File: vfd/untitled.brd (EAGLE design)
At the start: 128.9 x 185.7 mm, 80 parts, among them IC1 FSBB30CH60, IC2 74HCT04D, T1 BC547, X3 5202-06-N-02

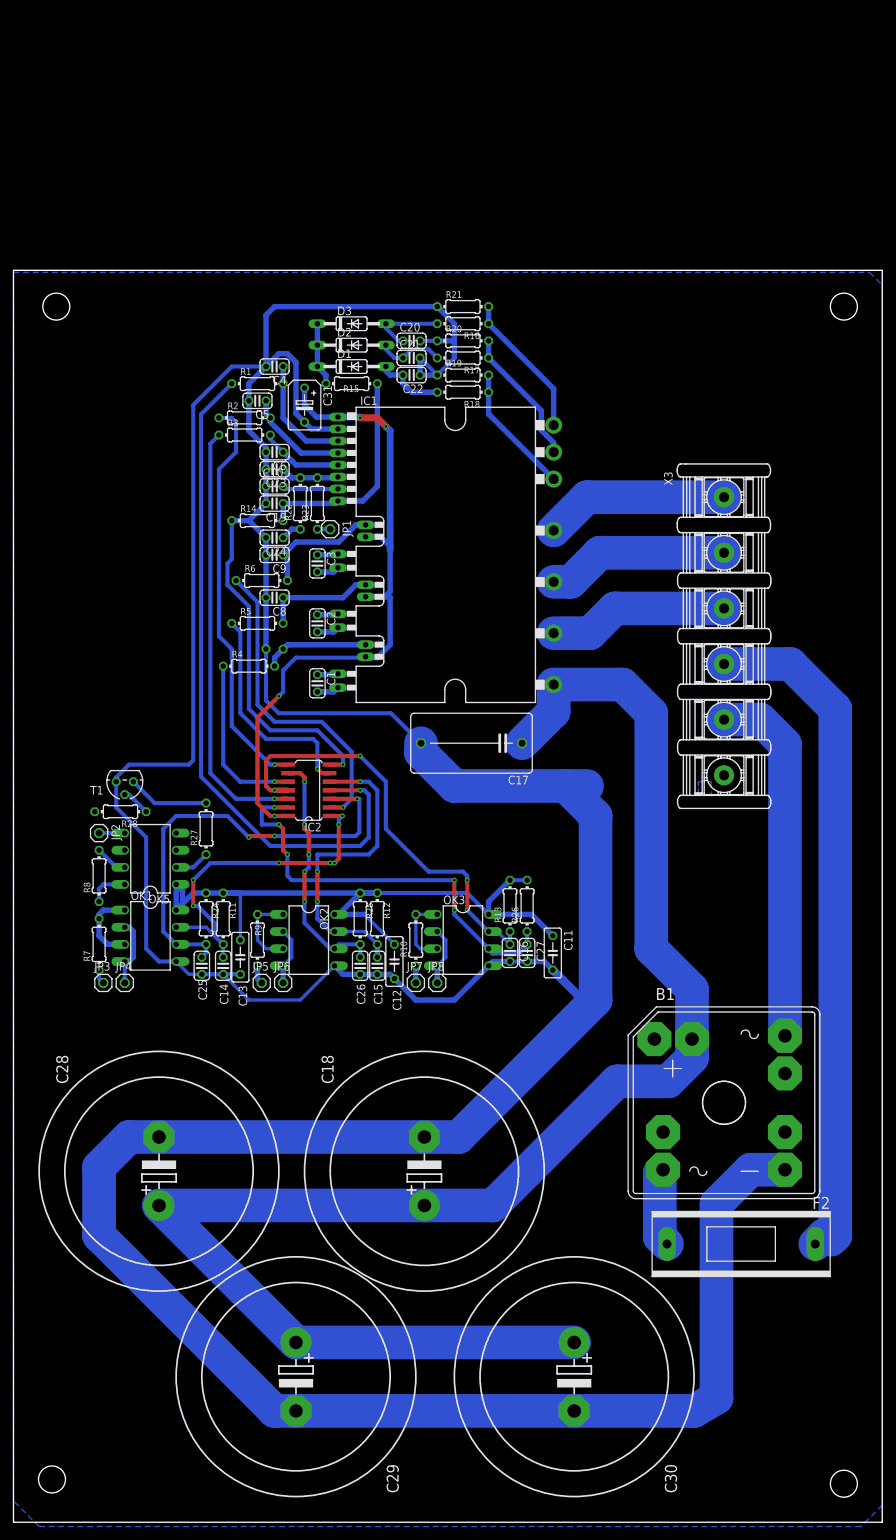
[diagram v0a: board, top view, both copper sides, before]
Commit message: update trafo
trafo 15v
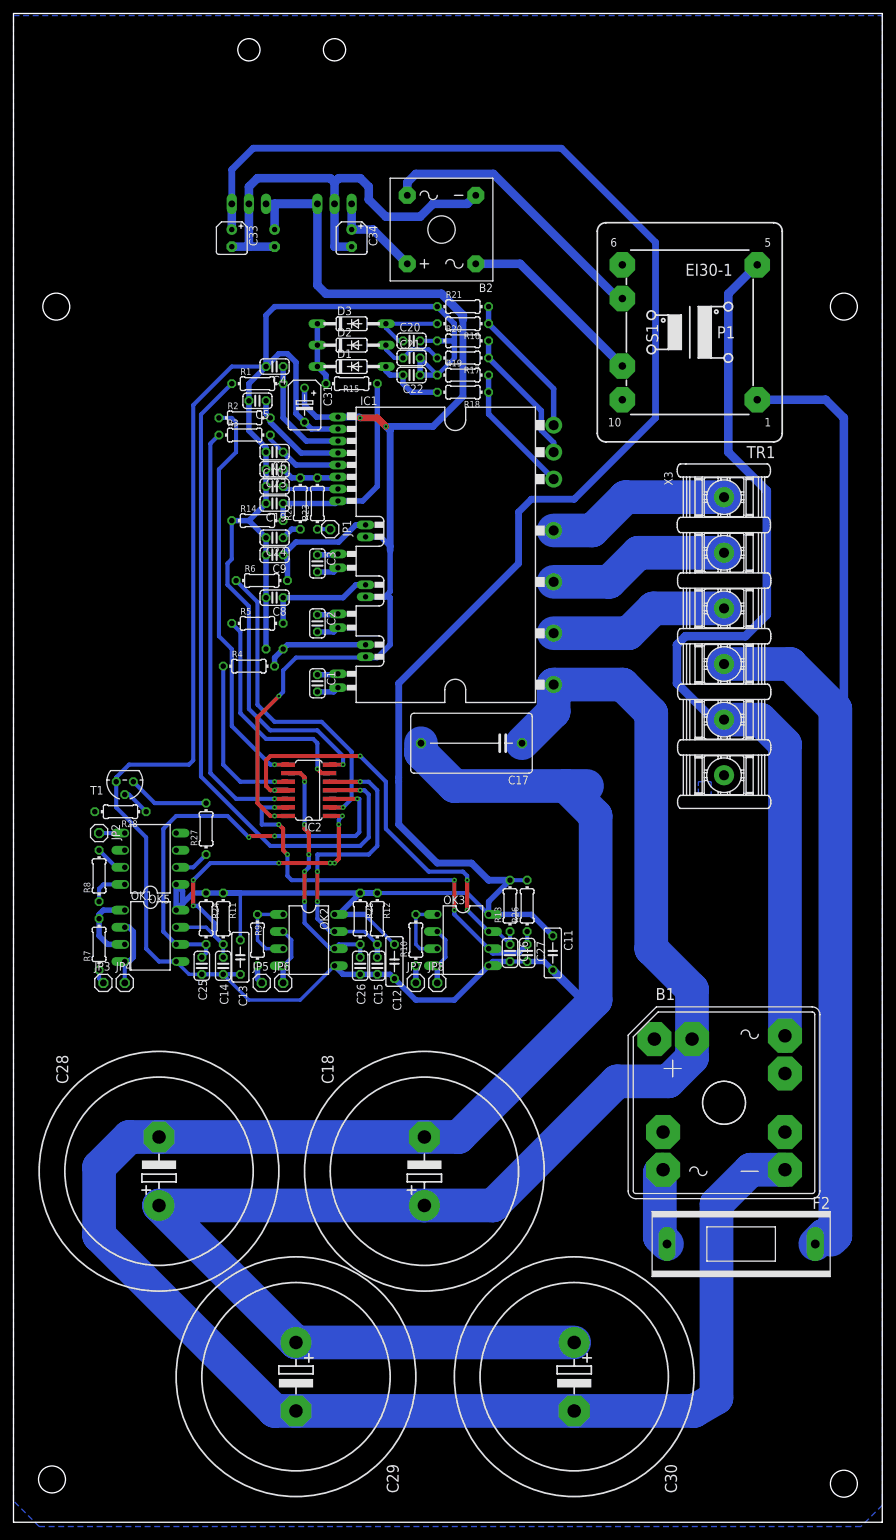
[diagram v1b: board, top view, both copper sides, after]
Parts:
- added B2: (no value), rectifier:S41
- added C32, C33, C34: (no value), rcl:B45181A
- added IC3: 15, v-reg:78MXXL
- added IC4: 5, v-reg:78MXXL
- added TR1: (no value), trafo:EI30-1
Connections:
- new net N$1: B2.AC1, TR1.9
- new net N$11: B2.-, C32.-, C33.-, C34.-, IC3.GND, IC4.GND
- new net N$3: B2.AC2, TR1.7
- new net N$7: B2.+, C34.+, IC3.IN
- net +15V: now also C32.+, IC3.OUT, IC4.IN
- net +5V: now also C33.+, IC4.OUT
- net L: now also TR1.1
- net N: now also TR1.5
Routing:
- net +5V: track 106.0 -> 310.7 mm
- net N: track 53.8 -> 140.0 mm
- net +15V: track 100.9 -> 179.5 mm
- net N$11: track 0.00 -> 66.8 mm
- net L: track 101.8 -> 159.4 mm
- net N$3: track 0.00 -> 42.0 mm
- net GND: track 709.2 -> 676.0 mm
- net N$1: track 0.00 -> 28.0 mm
- net N$7: track 0.00 -> 14.2 mm
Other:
- board size 128.9 x 185.7 mm -> 128.9 x 223.8 mm
